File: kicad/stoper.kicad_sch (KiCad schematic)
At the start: 16 parts

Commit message: finish up stoper schematics in kicad
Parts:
- added DefaultReset1: 1000 nF, symbol Device:C
- added DoubleSecondsCounter1, SingleSecondsCounter1: CD4026B, N16, symbol cd4026b:CD4026B
- added DoubleSecondsDisplay1, SingleSecondsDisplay1: HDSP-A403, Display_7Segment:HDSP-A401, symbol Display_Character:HDSP-A403
- added R10, R8: 220 Ohm, symbol Device:R
- added R11, R7, R9: 10 kOhm, symbol Device:R
- added Reset1: SW_SPST, symbol Switch:SW_SPST
- gave numbers to parts that had none: 1
- renumbered R7 to R6
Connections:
- net +9V: now also DefaultReset1.1, DoubleSecondsCounter1.16 (VDD), DoubleSecondsCounter1.3 (DISPLAYENABLEIN), Reset1.1 (A), SingleSecondsCounter1.16 (VDD), SingleSecondsCounter1.3 (DISPLAYENABLEIN)
- net GND: now also DoubleSecondsCounter1.14 (UNGATEDCSEGMENTOUT), DoubleSecondsCounter1.2 (CLOCKINHIBIT), DoubleSecondsCounter1.4 (DISPLAYENABLEOUT), DoubleSecondsCounter1.5 (CARRYOUT), DoubleSecondsCounter1.8 (VSS), R10.2, R11.2, R7.2, R8.2, R9.2, SingleSecondsCounter1.14 (UNGATEDCSEGMENTOUT), SingleSecondsCounter1.2 (CLOCKINHIBIT), SingleSecondsCounter1.4 (DISPLAYENABLEOUT), SingleSecondsCounter1.8 (VSS)
- net at MilliSecondsCounter1.15 (RESET): now also DefaultReset1.2, DoubleSecondsCounter1.15 (RESET), R11.1, R7.1, R9.1, Reset1.2 (B), SingleSecondsCounter1.15 (RESET)
- net at MilliSecondsCounter1.5 (CARRYOUT): now also SingleSecondsCounter1.1 (CLOCK)
- new net: DoubleSecondsCounter1.1 (CLOCK), SingleSecondsCounter1.5 (CARRYOUT)
- new net: DoubleSecondsCounter1.10 (A), DoubleSecondsDisplay1.10 (A)
- new net: DoubleSecondsCounter1.11 (E), DoubleSecondsDisplay1.4 (E)
- new net: DoubleSecondsCounter1.12 (B), DoubleSecondsDisplay1.9 (B)
- new net: DoubleSecondsCounter1.13 (C), DoubleSecondsDisplay1.8 (C)
- new net: DoubleSecondsCounter1.6 (F), DoubleSecondsDisplay1.2 (F)
- new net: DoubleSecondsCounter1.7 (G), DoubleSecondsDisplay1.3 (G)
- new net: DoubleSecondsCounter1.9 (D), DoubleSecondsDisplay1.5 (D)
- new net: SingleSecondsCounter1.10 (A), SingleSecondsDisplay1.10 (A)
- new net: SingleSecondsCounter1.11 (E), SingleSecondsDisplay1.4 (E)
- new net: SingleSecondsCounter1.12 (B), SingleSecondsDisplay1.9 (B)
- new net: SingleSecondsCounter1.13 (C), SingleSecondsDisplay1.8 (C)
- new net: SingleSecondsCounter1.6 (F), SingleSecondsDisplay1.2 (F)
- new net: SingleSecondsCounter1.7 (G), SingleSecondsDisplay1.3 (G)
- new net: SingleSecondsCounter1.9 (D), SingleSecondsDisplay1.5 (D)
- new net: R8.1, SingleSecondsDisplay1.6 (CC)
- new net: DoubleSecondsDisplay1.6 (CC), R10.1
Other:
- moved on the sheet: C1, DefaultOff1, MilliSecondsCounter1, MilliSecondsDisplay1, MillisecondsC1, MillisecondsTimer1, Off1, On1, OnOff1, OnOffLed1, R1, R2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

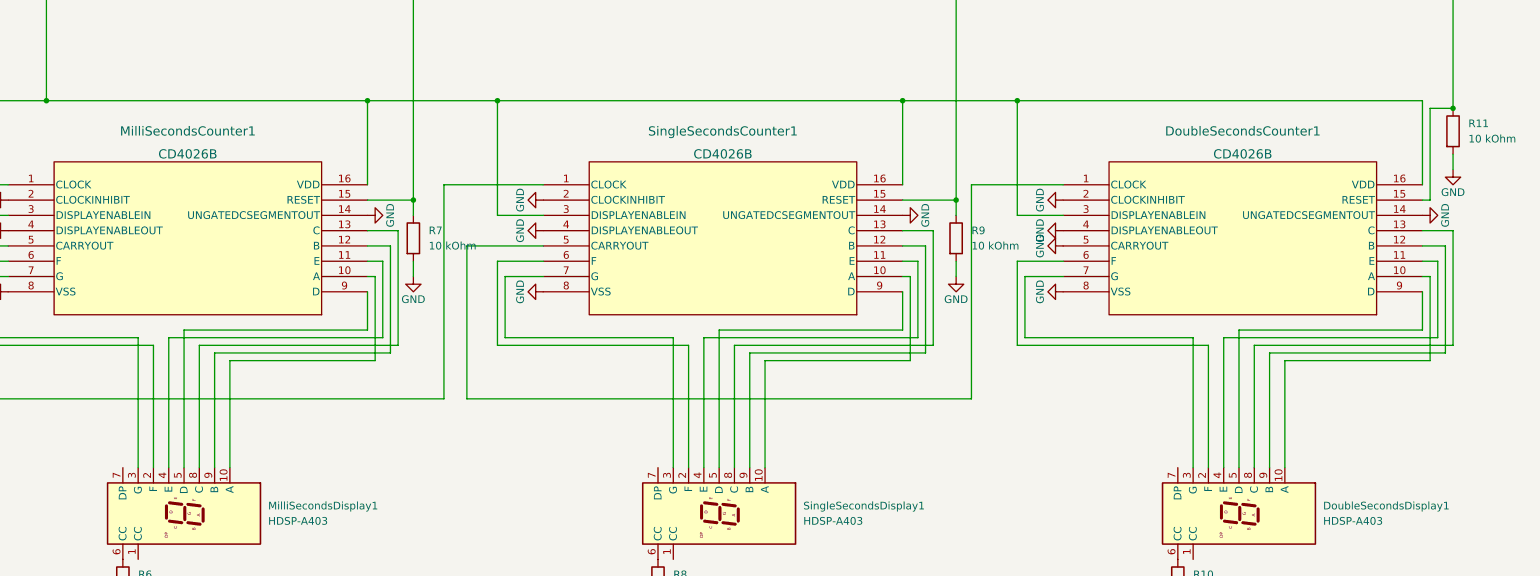
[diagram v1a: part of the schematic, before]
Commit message: update stoper schematics in kicad
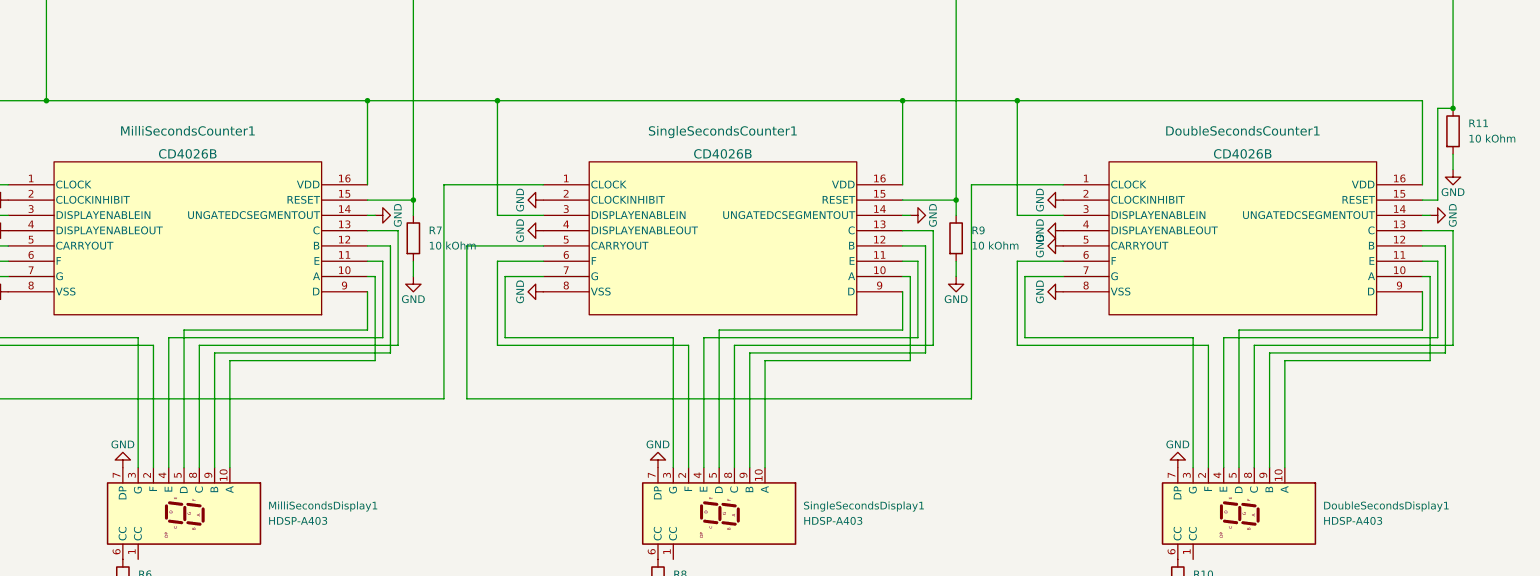
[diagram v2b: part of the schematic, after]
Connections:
- net GND: now also DoubleSecondsDisplay1.7 (DP), MilliSecondsDisplay1.7 (DP), SingleSecondsDisplay1.7 (DP)

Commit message: assign footprints to kicad proj
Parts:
- added R8: 220 Ohm, Resistor_THT:R_Axial_DIN0207_L6.3mm_D2.5mm_P10.16mm_Horizontal, symbol Device:R
- C1: footprint (none) -> Capacitor_THT:CP_Radial_D5.0mm_P2.50mm
- DefaultOff1, DefaultReset1, MillisecondsC1: footprint (none) -> Capacitor_THT:CP_Radial_D8.0mm_P5.00mm
- DoubleSecondsCounter1, MilliSecondsCounter1, SingleSecondsCounter1: footprint N16 -> Package_DIP:DIP-16_W10.16mm
- Off1, On1, OnOffLed1, Reset1: footprint (none) -> Button_Switch_THT:SW_PUSH_6mm
- R1, R2, R3, R4, R5, R6, R7: footprint (none) -> Resistor_THT:R_Axial_DIN0207_L6.3mm_D2.5mm_P10.16mm_Horizontal
- R10: renamed from R9; footprint (none) -> Resistor_THT:R_Axial_DIN0207_L6.3mm_D2.5mm_P10.16mm_Horizontal
- R11: renamed from R10; footprint (none) -> Resistor_THT:R_Axial_DIN0207_L6.3mm_D2.5mm_P10.16mm_Horizontal
- R12: renamed from R11; footprint (none) -> Resistor_THT:R_Axial_DIN0207_L6.3mm_D2.5mm_P10.16mm_Horizontal
- R9: renamed from R8; footprint (none) -> Resistor_THT:R_Axial_DIN0207_L6.3mm_D2.5mm_P10.16mm_Horizontal
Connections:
- net +9V: now also R8.2
- net GND: now also OnOff1.5 (CV), OnOff1.7 (DIS); no longer SingleSecondsDisplay1.7 (DP)
- net ResetButtonIn1: now reaches DefaultReset1.2, DoubleSecondsCounter1.15 (RESET), MilliSecondsCounter1.15 (RESET), R10.1, R12.1, R7.1, Reset1.2 (B), SingleSecondsCounter1.15 (RESET)
- net DoubleSecondsPulse1: now reaches DoubleSecondsCounter1.1 (CLOCK), SingleSecondsCounter1.5 (CARRYOUT)
- net SingleSecondsPulse1: now reaches MilliSecondsCounter1.5 (CARRYOUT), SingleSecondsCounter1.1 (CLOCK)
- net TimerPower1: now reaches MillisecondsTimer1.4 (R), MillisecondsTimer1.8 (VCC), OnOff1.3 (Q), OnOffLed1.2 (A), R4.1
- net MilliSecondsPulse1: now reaches MilliSecondsCounter1.1 (CLOCK), MillisecondsTimer1.3 (Q)
- new net: R8.1, SingleSecondsDisplay1.7 (DP)
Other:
- moved on the sheet: C1, DefaultReset1, MillisecondsC1, MillisecondsTimer1, R4, R5, Reset1

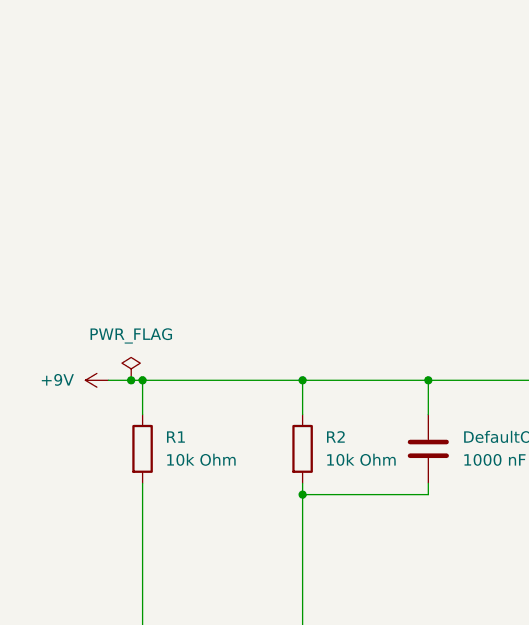
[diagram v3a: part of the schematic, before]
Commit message: improve footprints in kicad proj
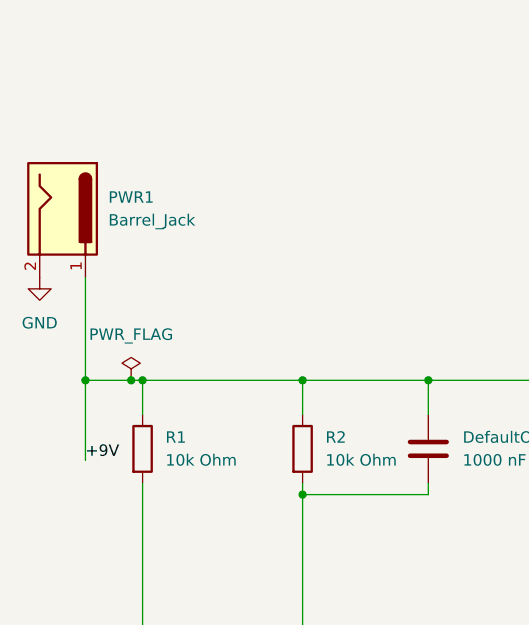
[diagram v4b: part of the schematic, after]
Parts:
- added PWR1: Barrel_Jack, Connector_BarrelJack:BarrelJack_GCT_DCJ200-10-A_Horizontal, symbol Connector:Barrel_Jack
- DoubleSecondsDisplay1, MilliSecondsDisplay1, SingleSecondsDisplay1: footprint Display_7Segment:HDSP-A401 -> Display_7Segment:7SegmentLED_LTS6760_LTS6780
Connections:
- net +9V: now also PWR1.1
- net GND: now also PWR1.2
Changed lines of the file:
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@@
   (junction (at 134.62 22.86) (diameter 0) (color 0 0 0 0)
   )
+  (junction (at 21.59 63.5) (diameter 0) (color 0 0 0 0)
+  )
   (junction (at 224.79 63.5) (diameter 0) (color 0 0 0 0)
   )
@@
     (stroke (width 0) (type default) (color 0 0 0 0))
   )
+  (wire (pts (xy 21.59 63.5) (xy 21.59 52.07))
+    (stroke (width 0) (type default) (color 0 0 0 0))
+  )
   (wire (pts (xy 104.14 133.35) (xy 104.14 130.81))
     (stroke (width 0) (type default) (color 0 0 0 0))
@@
     (stroke (width 0) (type default) (color 0 0 0 0))
   )
+  (wire (pts (xy 21.59 63.5) (xy 21.59 72.39))
+    (stroke (width 0) (type default) (color 0 0 0 0))
+  )
   (wire (pts (xy 91.44 163.83) (xy 105.41 163.83))
     (stroke (width 0) (type default) (color 0 0 0 0))
@@
     (stroke (width 0) (type default) (color 0 0 0 0))
   )
-  (wire (pts (xy 24.13 63.5) (xy 26.67 63.5))
+  (wire (pts (xy 21.59 63.5) (xy 26.67 63.5))
     (stroke (width 0) (type default) (color 0 0 0 0))
   )
@@
   )
   (label "SingleSecondsPulse1" (at 251.46 77.47 90)
+    (effects (font (size 1.27 1.27)) (justify left bottom))
+  )
+  (label "+9V" (at 21.59 72.39 0)
     (effects (font (size 1.27 1.27)) (justify left bottom))
   )
@@
     (pin "1")
   )
-  (symbol (lib_id "power:+9V") (at 24.13 63.5 90) (unit 1)
-    (in_bom yes) (on_board yes) (fields_autoplaced)
-    (property "Reference" "#PWR01" (id 0) (at 27.94 63.5 0)
-      (effects (font (size 1.27 1.27)) hide)
-    )
-    (property "Value" "+9V" (id 1) (at 20.32 63.4999 90)
-      (effects (font (size 1.27 1.27)) (justify left))
-    )
-    (property "Footprint" "" (id 2) (at 24.13 63.5 0)
-      (effects (font (size 1.27 1.27)) hide)
-    )
-    (property "Datasheet" "" (id 3) (at 24.13 63.5 0)
-      (effects (font (size 1.27 1.27)) hide)
-    )
-    (pin "1")
-  )
   (symbol (lib_id "power:GND") (at 226.06 82.55 90) (unit 1)
     (in_bom yes) (on_board yes)
@@
       (effects (font (size 1.27 1.27)) (justify left))
     )
-    (property "Footprint" "Display_7Segment:HDSP-A401" (id 2) (at 269.24 132.08 0)
+    (property "Footprint" "Display_7Segment:7SegmentLED_LTS6760_LTS6780" (id 2) (at 269.24 132.08 0)
       (effects (font (size 1.27 1.27)) hide)
     )
@@
     (pin "9")
   )
+  (symbol (lib_id "power:GND") (at 16.51 52.07 0) (unit 1)
+    (in_bom yes) (on_board yes) (fields_autoplaced)
+    (property "Reference" "#PWR01" (id 0) (at 16.51 58.42 0)
+      (effects (font (size 1.27 1.27)) hide)
+    )
+    (property "Value" "GND" (id 1) (at 16.51 57.15 0))
+    (property "Footprint" "" (id 2) (at 16.51 52.07 0)
+      (effects (font (size 1.27 1.27)) hide)
+    )
+    (property "Datasheet" "" (id 3) (at 16.51 52.07 0)
+      (effects (font (size 1.27 1.27)) hide)
+    )
+    (pin "1")
+  )
   (symbol (lib_id "power:GND") (at 184.15 147.32 0) (unit 1)
     (in_bom yes) (on_board yes) (fields_autoplaced)
@@
     )
     (pin "1")
+  )
+  (symbol (lib_id "Connector:Barrel_Jack") (at 19.05 44.45 270) (unit 1)
+    (in_bom yes) (on_board yes) (fields_autoplaced)
+    (property "Reference" "PWR1" (id 0) (at 24.13 43.1799 90)
+      (effects (font (size 1.27 1.27)) (justify left))
+    )
+    (property "Value" "Barrel_Jack" (id 1) (at 24.13 45.7199 90)
+      (effects (font (size 1.27 1.27)) (justify left))
+    )
+    (property "Footprint" "Connector_BarrelJack:BarrelJack_GCT_DCJ200-10-A_Horizontal" (id 2) (at 18.034 45.72 0)
+      (effects (font (size 1.27 1.27)) hide)
+    )
+    (property "Datasheet" "~" (id 3) (at 18.034 45.72 0)
+      (effects (font (size 1.27 1.27)) hide)
+    )
+    (pin "1")
+    (pin "2")
   )
   (symbol (lib_id "Device:R") (at 104.14 127 0) (unit 1)
@@
       (effects (font (size 1.27 1.27)) (justify left))
     )
-    (property "Footprint" "Display_7Segment:HDSP-A401" (id 2) (at 355.6 132.08 0)
+    (property "Footprint" "Display_7Segment:7SegmentLED_LTS6760_LTS6780" (id 2) (at 355.6 132.08 0)
       (effects (font (size 1.27 1.27)) hide)
     )
@@
       (effects (font (size 1.27 1.27)) (justify left))
     )
-    (property "Footprint" "Display_7Segment:HDSP-A401" (id 2) (at 180.34 132.08 0)
+    (property "Footprint" "Display_7Segment:7SegmentLED_LTS6760_LTS6780" (id 2) (at 180.34 132.08 0)
       (effects (font (size 1.27 1.27)) hide)
     )
@@
       (reference "#FLG01") (unit 1) (value "PWR_FLAG") (footprint "")
     )
-    (path "/425b3b4d-9a18-4c10-9fe2-354862a35ffd"
-      (reference "#PWR01") (unit 1) (value "+9V") (footprint "")
+    (path "/64ffa6bf-c0bf-4f57-a899-cad4c8926679"
+      (reference "#PWR01") (unit 1) (value "GND") (footprint "")
     )
     (path "/e6a5c50a-ede6-48aa-9bc7-07603e23dc71"
@@
     )
     (path "/a7b58b90-7880-416e-95e5-e6cff1d964be"
-      (reference "DoubleSecondsDisplay1") (unit 1) (value "HDSP-A403") (footprint "Display_7Segment:HDSP-A401")
+      (reference "DoubleSecondsDisplay1") (unit 1) (value "HDSP-A403") (footprint "Display_7Segment:7SegmentLED_LTS6760_LTS6780")
     )
     (path "/ebe9f24a-f182-40ed-af70-9a9f559aea3b"
@@
     )
     (path "/c5b5257d-3ea0-461e-bd1b-67115b9f7bd2"
-      (reference "MilliSecondsDisplay1") (unit 1) (value "HDSP-A403") (footprint "Display_7Segment:HDSP-A401")
+      (reference "MilliSecondsDisplay1") (unit 1) (value "HDSP-A403") (footprint "Display_7Segment:7SegmentLED_LTS6760_LTS6780")
     )
     (path "/b06647d0-e677-4895-a7fd-ff108f97cc82"
@@
       (reference "OnOffLed1") (unit 1) (value "LED") (footprint "Button_Switch_THT:SW_PUSH_6mm")
     )
+    (path "/958e37ef-b599-4840-8e6d-586dd7ec27ce"
+      (reference "PWR1") (unit 1) (value "Barrel_Jack") (footprint "Connector_BarrelJack:BarrelJack_GCT_DCJ200-10-A_Horizontal")
+    )
     (path "/33bb8cb0-2cdb-464a-abfe-cb448b6e57fe"
       (reference "R1") (unit 1) (value "10k Ohm") (footprint "Resistor_THT:R_Axial_DIN0207_L6.3mm_D2.5mm_P10.16mm_Horizontal")
@@
     )
     (path "/5c41fcf1-e87d-4b56-9b03-d956ba0926ee"
-      (reference "SingleSecondsDisplay1") (unit 1) (value "HDSP-A403") (footprint "Display_7Segment:HDSP-A401")
-    )
-  )
+      (reference "SingleSecondsDisplay1") (unit 1) (value "HDSP-A403") (footprint "Display_7Segment:7SegmentLED_LTS6760_LTS6780")
+    )
+  )

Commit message: save pcb layout draft
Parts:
- OnOffLed1: footprint Button_Switch_THT:SW_PUSH_6mm -> LED_THT:LED_D5.0mm
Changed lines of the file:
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@@
       (effects (font (size 1.27 1.27)) (justify right))
     )
-    (property "Footprint" "Button_Switch_THT:SW_PUSH_6mm" (id 2) (at 104.14 115.57 0)
+    (property "Footprint" "LED_THT:LED_D5.0mm" (id 2) (at 104.14 115.57 0)
       (effects (font (size 1.27 1.27)) hide)
     )
@@
     )
     (path "/1b96be94-e01f-48ed-805c-c6c0db9e0f9e"
-      (reference "OnOffLed1") (unit 1) (value "LED") (footprint "Button_Switch_THT:SW_PUSH_6mm")
+      (reference "OnOffLed1") (unit 1) (value "LED") (footprint "LED_THT:LED_D5.0mm")
     )
     (path "/958e37ef-b599-4840-8e6d-586dd7ec27ce"
